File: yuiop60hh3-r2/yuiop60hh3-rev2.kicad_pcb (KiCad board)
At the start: 2 copper layers, 285 x 94.6 mm, 159 parts, among them J1 USB_B_Micro, J2 ISP, U1 ATmega32U4-AU, X1 XTAL

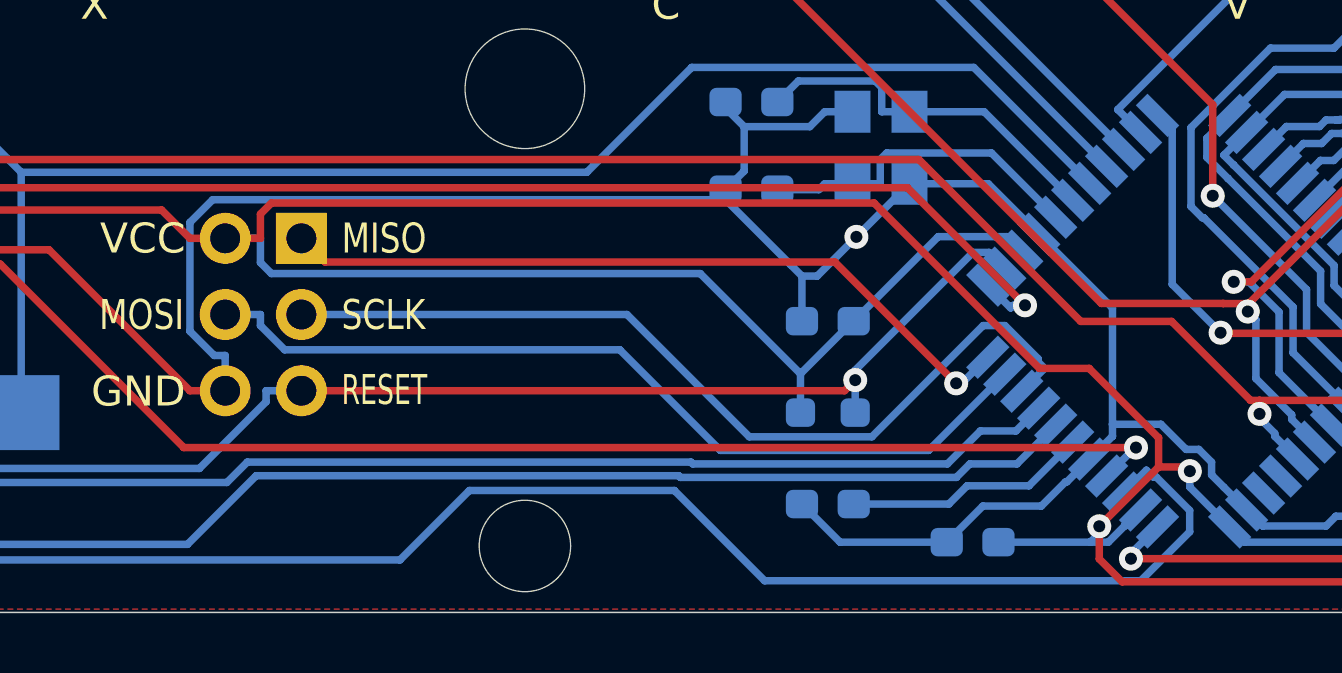
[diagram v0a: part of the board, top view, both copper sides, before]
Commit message: yuiop60hh3-rev2: reduce via
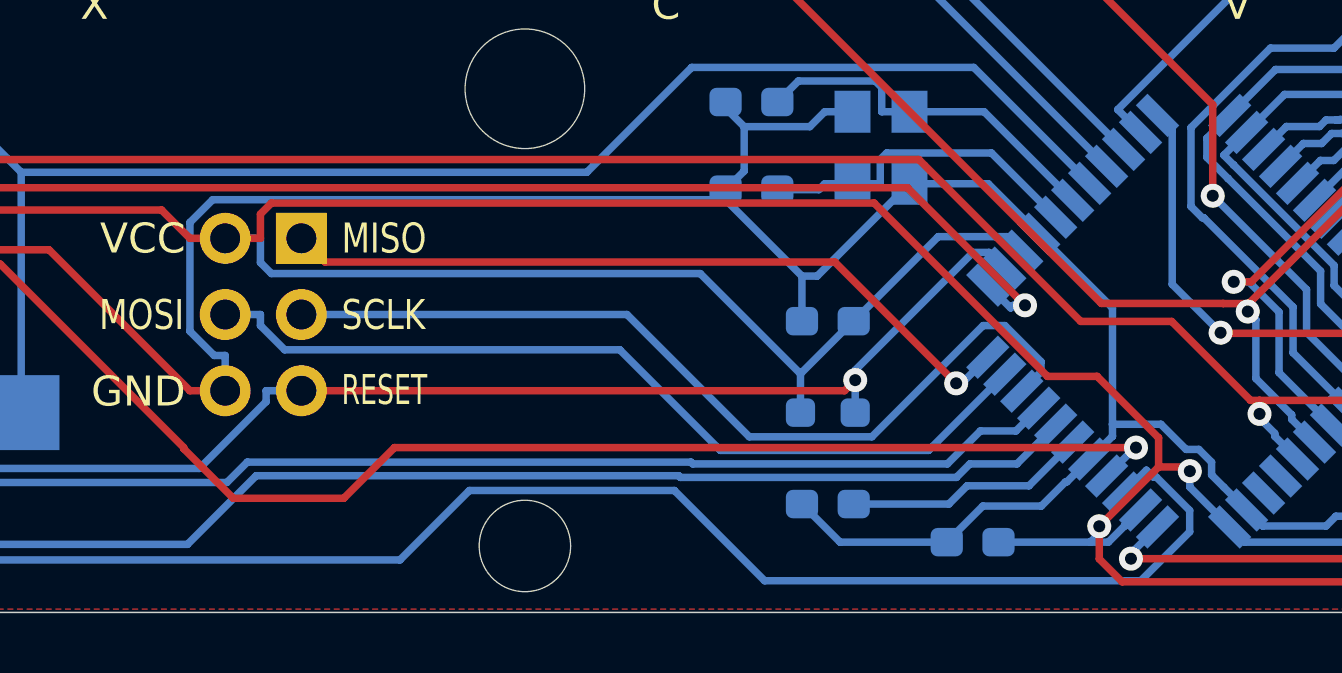
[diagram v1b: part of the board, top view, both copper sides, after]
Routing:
- net /Controller/D+: track 92.5 -> 94.0 mm
- net GND: vias 4 -> 3
